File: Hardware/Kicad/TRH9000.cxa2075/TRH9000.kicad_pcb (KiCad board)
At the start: 4 copper layers, 100 x 77.5 mm, 62 parts, among them J1 S-Video, J2 RGB, Q1 BC817, U1 74HC138, U2 74HC32, U3 V9990, U4 KM428C256, U5 KM428C256, U6 CXA2075M, X1 14.31818MHz, Y1 21.47727Mhz

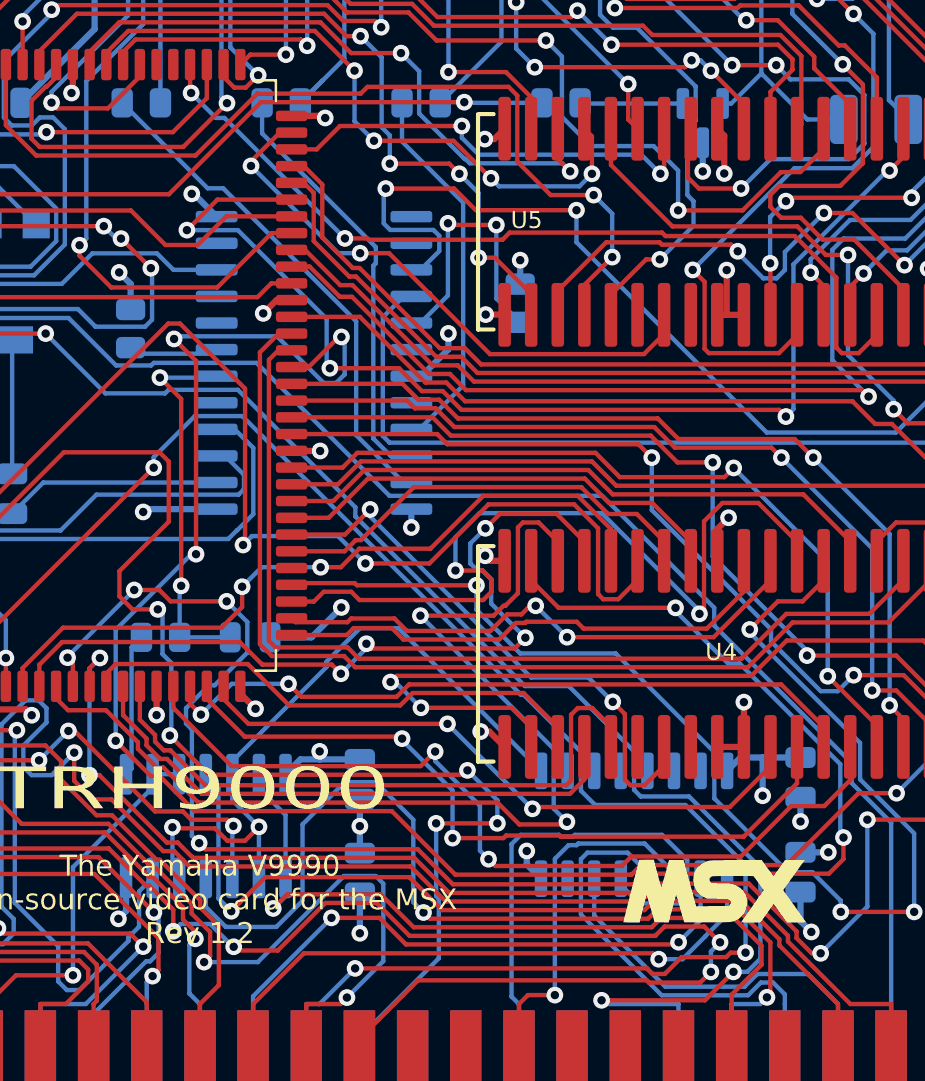
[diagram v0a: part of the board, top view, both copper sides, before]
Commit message: Fix on VRAM wiring
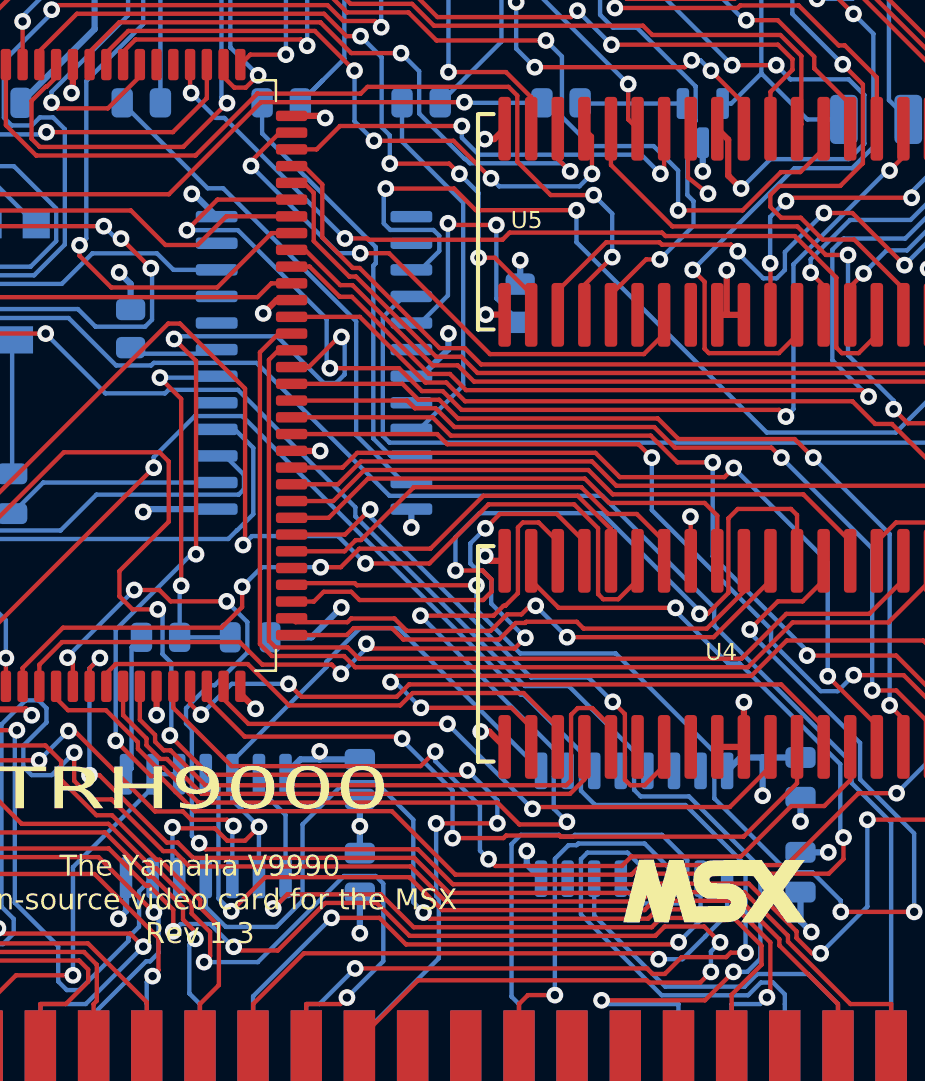
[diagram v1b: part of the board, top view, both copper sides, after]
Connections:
- U4 pad 12: GND -> /VDP/~{V0_WE}
- U4 pad 13: /VDP/~{V0_WE} -> GND
- U5 pad 12: GND -> /VDP/~{V1_WE}
- U5 pad 13: /VDP/~{V1_WE} -> GND
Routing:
- net /VDP/~{V0_WE}: track 22.0 -> 24.0 mm
- net /VDP/~{V1_WE}: track 56.5 -> 54.7 mm
- net GND: track 116.0 -> 117.1 mm
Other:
- board text added: "The Yamaha V9990 open-source video card for the MSX Rev 1.3"
- board text removed: "The Yamaha V9990 open-source video card for the MSX Rev 1.2"

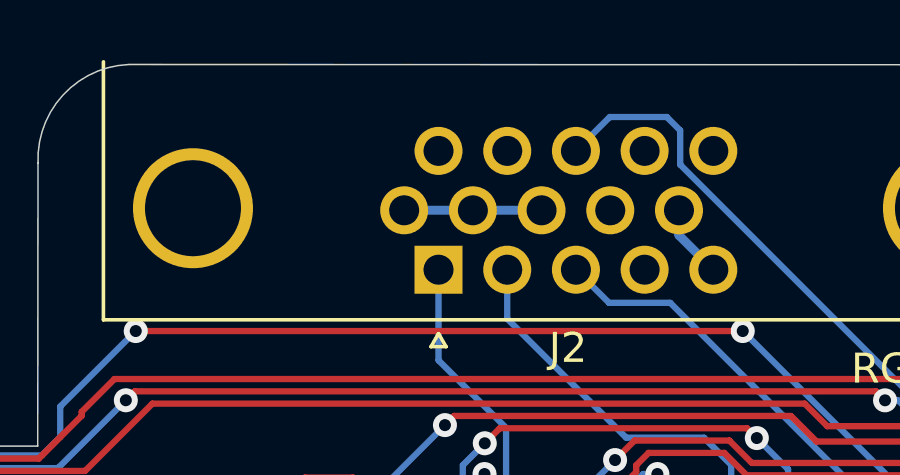
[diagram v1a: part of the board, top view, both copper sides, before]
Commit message: Jumper to provide 5V to SCART cables
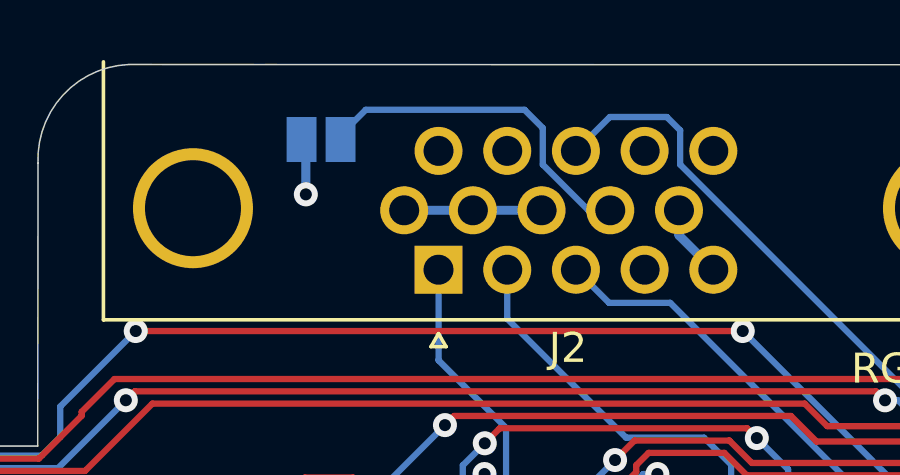
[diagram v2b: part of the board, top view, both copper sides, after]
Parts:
- added JP1: Jumper_2_Open, Jumper:SolderJumper-2_P1.3mm_Open_Pad1.0x1.5mm, B.Cu at (143.2, 58.5)
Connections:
- J2 pad 9: unconnected-(J2-P9-Pad9) -> Net-(J2-P9)
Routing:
- net Net-(J2-P9): track 0.00 -> 11.7 mm
- net +5V: track 106.5 -> 108.5 mm, vias 25 -> 26
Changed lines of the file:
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@@
   (net 92 "/VDP/V1S1")
   (net 93 "/VDP/V1S0")
-  (net 94 "unconnected-(J2-P9-Pad9)")
+  (net 94 "Net-(J2-P9)")
   (net 95 "Net-(C11-Pad1)")
   (net 96 "/VDP/V1A8")
@@
       (net 1 "GND") (pinfunction "8") (pintype "passive"))
     (pad "9" thru_hole circle (at -5.725 1.98 180) (size 1.6 1.6) (drill 1) (layers "*.Cu" "*.Mask")
-      (net 94 "unconnected-(J2-P9-Pad9)") (pinfunction "P9") (pintype "passive+no_connect"))
+      (net 94 "Net-(J2-P9)") (pinfunction "P9") (pintype "passive"))
     (pad "10" thru_hole circle (at -8.015 1.98 180) (size 1.6 1.6) (drill 1) (layers "*.Cu" "*.Mask")
       (net 1 "GND") (pinfunction "P10") (pintype "passive"))
@@
     )
   )
+  (footprint "Jumper:SolderJumper-2_P1.3mm_Open_Pad1.0x1.5mm" (layer "B.Cu")
+    (at 143.2052 58.4708)
+    (descr "SMD Solder Jumper, 1x1.5mm Pads, 0.3mm gap, open")
+    (tags "solder jumper open")
+    (property "Sheetfile" "TRH9000_VIDEO.kicad_sch")
+    (property "Sheetname" "VIDEO")
+    (property "ki_description" "Jumper, 2-pole, open")
+    (property "ki_keywords" "Jumper SPST")
+    (attr exclude_from_pos_files)
+    (fp_text reference "JP1" (at 0 1.8) (layer "B.SilkS")
+        (effects (font (size 1 1) (thickness 0.15)) (justify mirror))
+    )
+    (fp_text value "Jumper_2_Open" (at 0 -1.9) (layer "B.Fab")
+        (effects (font (size 1 1) (thickness 0.15)) (justify mirror))
+    )
+    (fp_line (start -1.4 -1) (end -1.4 1)
+      (stroke (width 0.12) (type solid)) (layer "B.SilkS"))
+    (fp_line (start -1.4 1) (end 1.4 1)
+      (stroke (width 0.12) (type solid)) (layer "B.SilkS"))
+    (fp_line (start 1.4 -1) (end -1.4 -1)
+      (stroke (width 0.12) (type solid)) (layer "B.SilkS"))
+    (fp_line (start 1.4 1) (end 1.4 -1)
+      (stroke (width 0.12) (type solid)) (layer "B.SilkS"))
+    (fp_line (start -1.65 1.25) (end -1.65 -1.25)
+      (stroke (width 0.05) (type solid)) (layer "B.CrtYd"))
+    (fp_line (start -1.65 1.25) (end 1.65 1.25)
+      (stroke (width 0.05) (type solid)) (layer "B.CrtYd"))
+    (fp_line (start 1.65 -1.25) (end -1.65 -1.25)
+      (stroke (width 0.05) (type solid)) (layer "B.CrtYd"))
+    (fp_line (start 1.65 -1.25) (end 1.65 1.25)
+      (stroke (width 0.05) (type solid)) (layer "B.CrtYd"))
+    (pad "1" smd rect (at -0.65 0) (size 1 1.5) (layers "B.Cu" "B.Mask")
+      (net 4 "+5V") (pinfunction "A") (pintype "passive"))
+    (pad "2" smd rect (at 0.65 0) (size 1 1.5) (layers "B.Cu" "B.Mask")
+      (net 94 "Net-(J2-P9)") (pinfunction "B") (pintype "passive"))
+  )
   (footprint "Resistor_SMD:R_0805_2012Metric" (layer "B.Cu")
     (at 117.348 73.0015 90)
@@
   (segment (start 190.81 85.26) (end 185.585 80.035) (width 0.3) (layer "F.Cu") (net 4))
   (segment (start 195.54 115.2) (end 196.565 114.175) (width 0.3) (layer "F.Cu") (net 4))
+  (via (at 142.6972 60.2996) (size 0.8) (drill 0.4) (layers "F.Cu" "B.Cu") (free) (net 4))
   (via (at 154.54 118.4677) (size 0.8) (drill 0.4) (layers "F.Cu" "B.Cu") (net 4))
   (via (at 149.9249 88.8558) (size 0.8) (drill 0.4) (layers "F.Cu" "B.Cu") (net 4))
@@
   (segment (start 117.348 94.1221) (end 117.348 91.4475) (width 0.3) (layer "B.Cu") (net 4))
   (segment (start 117.348 100.9125) (end 117.348 99.7741) (width 0.3) (layer "B.Cu") (net 4))
+  (segment (start 142.6972 60.2996) (end 142.6972 58.7652) (width 0.3) (layer "B.Cu") (net 4))
   (segment (start 143.59 87.446) (end 143.043 86.899) (width 0.3) (layer "B.Cu") (net 4))
   (segment (start 130.2273 119.9725) (end 130.2273 121.8027) (width 0.3) (layer "B.Cu") (net 4))
+  (segment (start 142.6972 58.7652) (end 142.4028 58.4708) (width 0.3) (layer "B.Cu") (net 4))
   (segment (start 129.12 127.653) (end 129.12 121.8027) (width 0.3) (layer "B.Cu") (net 4))
   (segment (start 157 91.855) (end 157.4824 91.855) (width 0.3) (layer "B.Cu") (net 4))
@@
   (segment (start 154.2027 86.6855) (end 152.7462 85.229) (width 0.21) (layer "F.Cu") (net 93))
   (segment (start 182.0175 82.5155) (end 182.0175 83.0997) (width 0.21) (layer "F.Cu") (net 93))
+  (segment (start 150.595 58.0882) (end 150.595 59.308006) (width 0.21) (layer "B.Cu") (net 94))
+  (segment (start 152.117294 60.8303) (end 152.845 60.8303) (width 0.21) (layer "B.Cu") (net 94))
+  (segment (start 149.987 57.4802) (end 150.595 58.0882) (width 0.21) (layer "B.Cu") (net 94))
+  (segment (start 150.595 59.308006) (end 152.117294 60.8303) (width 0.21) (layer "B.Cu") (net 94))
+  (segment (start 143.7028 58.4708) (end 144.6934 57.4802) (width 0.21) (layer "B.Cu") (net 94))
+  (segment (start 144.6934 57.4802) (end 149.987 57.4802) (width 0.21) (layer "B.Cu") (net 94))
   (segment (start 145.0125 78.7975) (end 145.012 78.7975) (width 0.21) (layer "B.Cu") (net 95))
   (segment (start 146.2977 71.8202) (end 145.012 73.105) (width 0.21) (layer "B.Cu") (net 95))

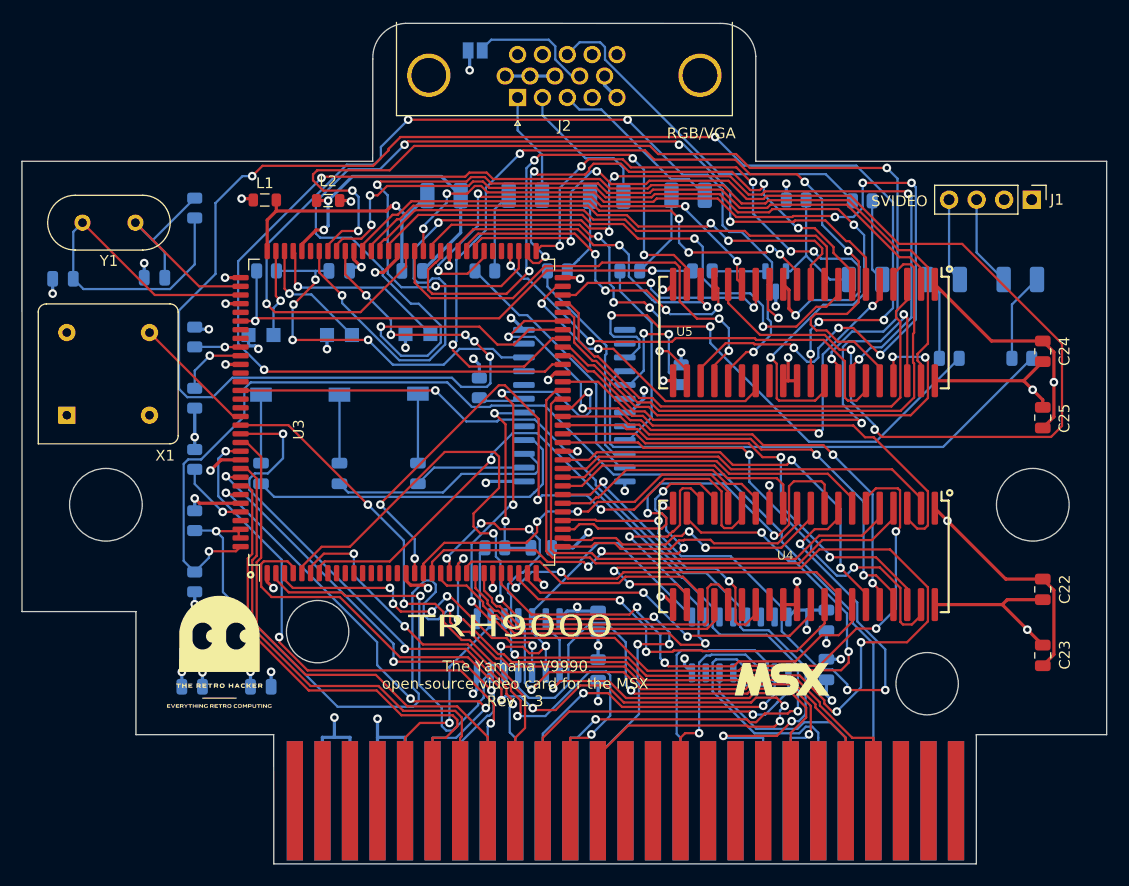
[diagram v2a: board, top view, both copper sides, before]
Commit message: Exposing composite, footprint and silk corrections
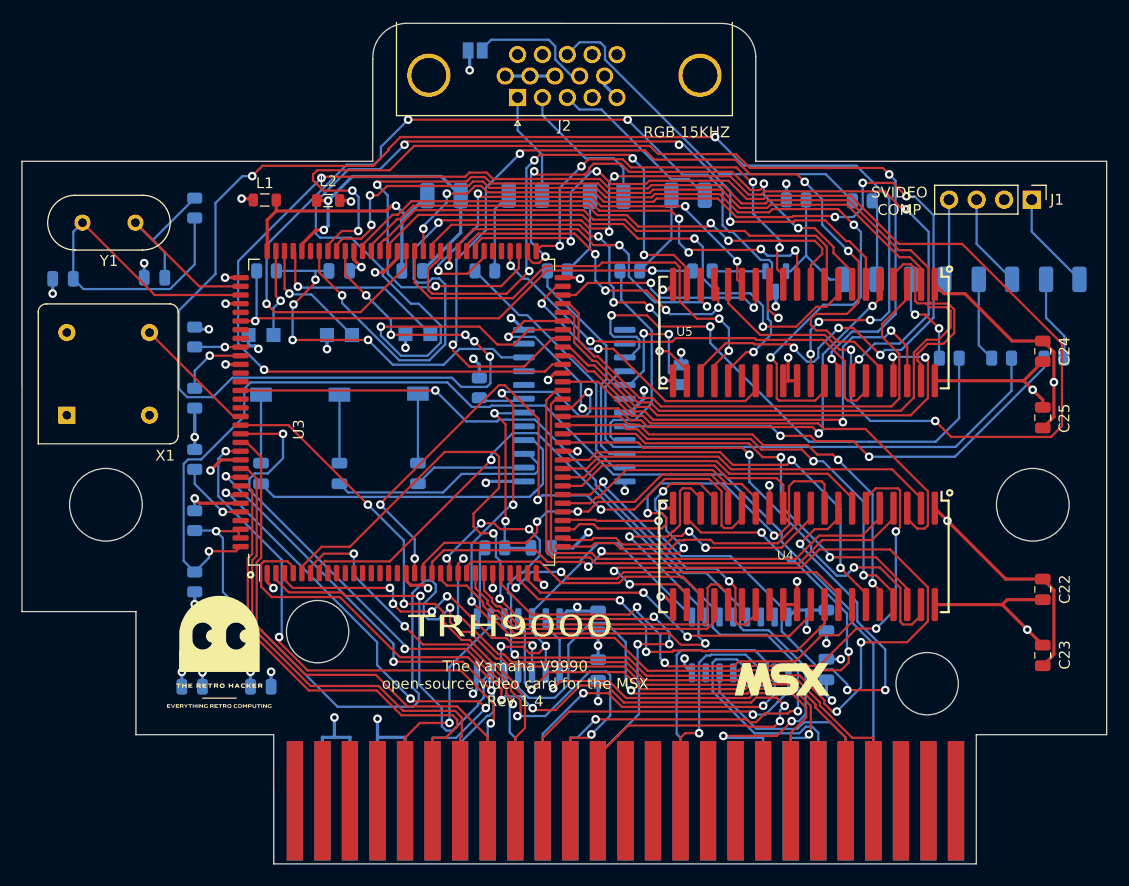
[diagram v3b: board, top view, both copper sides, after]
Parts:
- added C26: 220uF, Capacitor_Tantalum_SMD:CP_EIA-3528-15_AVX-H, B.Cu at (197.4, 79.6)
- added R19: 75R, Resistor_SMD:R_0805_2012Metric, B.Cu at (196.6, 86.8)
- added REF**: OSHW-Logo2_24.3x20mm_SilkScreen, Symbol:OSHW-Logo2_24.3x20mm_SilkScreen, B.Cu at (174.5, 95.6)
- moved C14 2.29 mm to (191.2, 79.6), turned to 0 degrees
- moved R17 1.86 mm to (191.7, 86.8)
- moved C15 1.43 mm to (184.9, 79.6)
- moved C9 0.52 mm to (178.7, 79.6)
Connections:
- J1 pad 1: GND -> /VIDEO/CVOUT
- U6 pad 20: unconnected-(U6-CVOUT-Pad20) -> Net-(U6-CVOUT)
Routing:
- net Net-(U6-CVOUT): track 0.00 -> 44.1 mm, vias 0 -> 2
- net /VDP/~{V1_WE}: track 54.7 -> 38.3 mm, vias 6 -> 4
- net /VIDEO/CVOUT: track 0.00 -> 9.17 mm
- net Net-(C26-Pad1): track 0.00 -> 7.99 mm
- net /VDP/V1S6: track 51.2 -> 45.6 mm
- net /VDP/V1S1: track 53.4 -> 58.1 mm
- net /VDP/V1S7: track 121.0 -> 124.7 mm
- net Net-(U6-COUT): track 48.0 -> 51.3 mm
- net Net-(U6-BOUT): track 18.1 -> 20.7 mm
- net /VDP/V1A2: track 93.1 -> 94.8 mm
- net /VDP/V1D3: track 47.7 -> 49.2 mm
- net /VDP/V1D7: track 102.8 -> 104.0 mm
- net Net-(C15-Pad1): track 7.76 -> 8.90 mm, vias 0 -> 2
- net /VDP/V1S0: track 47.9 -> 48.9 mm
- net /VDP/V1D6: track 91.8 -> 91.1 mm
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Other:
- board text added: "RGB 15KHZ"
- board text added: "SVIDEO COMP"
- board text added: "The Yamaha V9990 open-source video card for the MSX Rev 1.4"
- board text removed: "RGB/VGA"
- board text removed: "SVIDEO"
- board text removed: "The Yamaha V9990 open-source video card for the MSX Rev 1.3"
